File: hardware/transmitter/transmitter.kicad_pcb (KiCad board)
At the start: 2 copper layers, 69.1 x 53.8 mm, 25 parts, among them J1 Output

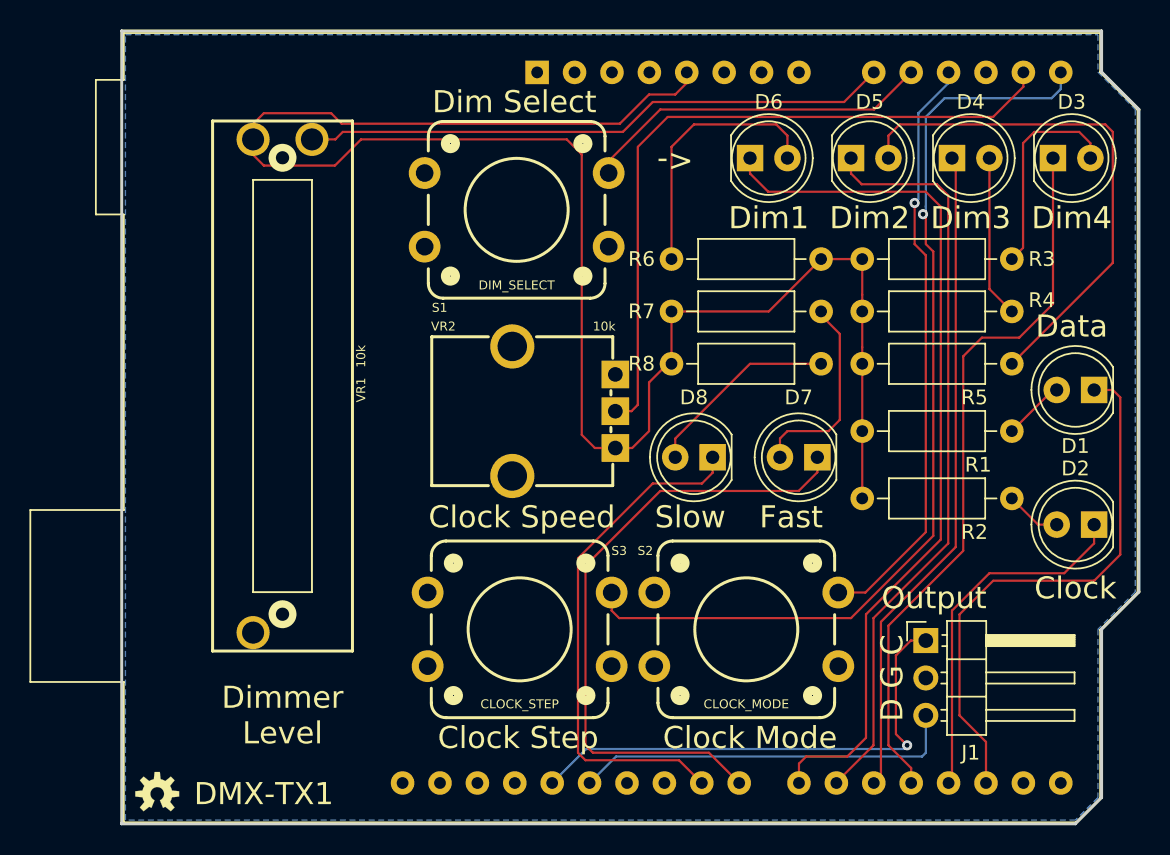
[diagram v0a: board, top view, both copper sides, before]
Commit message: Rev 1.1: - Fixed arduino shield footprint (it was backwards) - Added Fcu power plane - New Fcu layouts - Added rounded corners
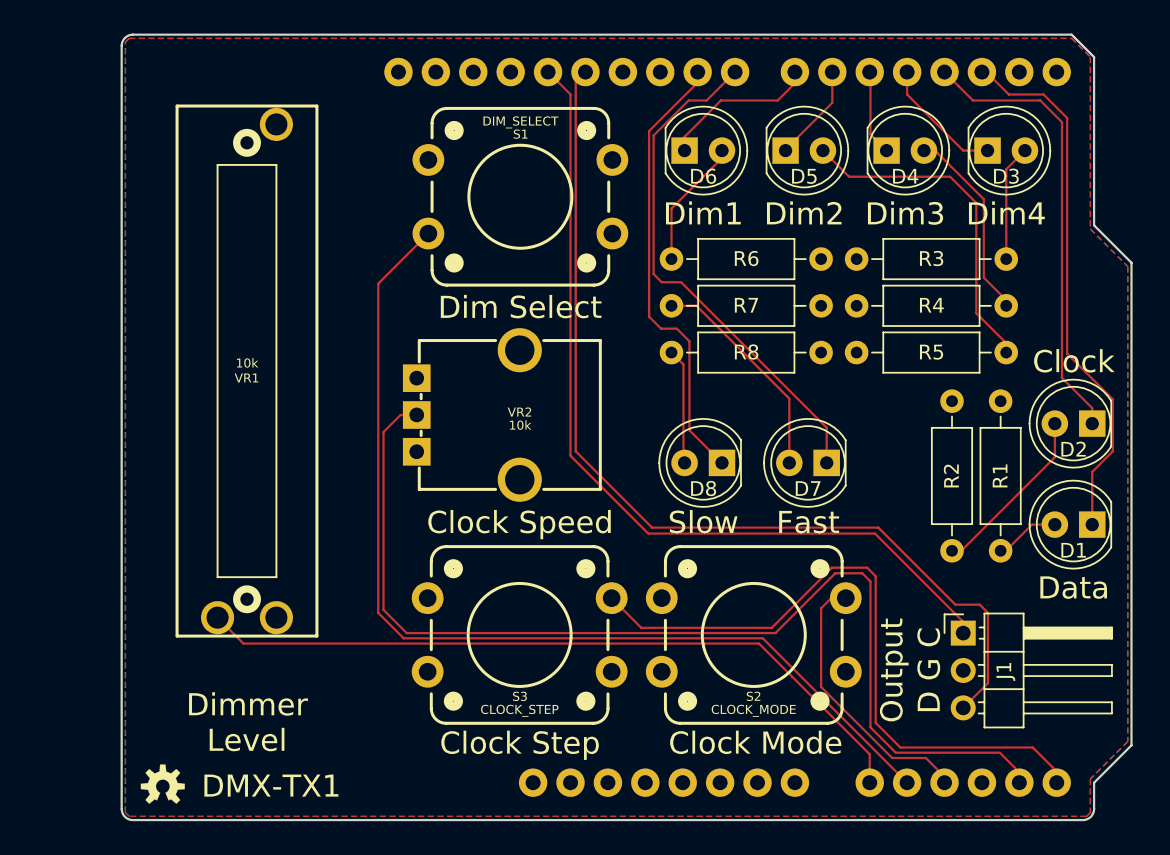
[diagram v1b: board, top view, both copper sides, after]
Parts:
- removed the ? at (118.7, 114.8)
- added ?: , footprints:OSHW-LOGO-S, F.Cu at (119.1, 114.3)
- A1: footprint Module:Arduino_UNO_R3 -> footprints:ARDUINO_R3_NO_HOLES
- moved A1 24.9 mm to (150.6, 89.9)
- moved R8 10.2 mm to (163.8, 84.8), turned to 180 degrees
- moved R7 10.2 mm to (163.8, 81.7), turned to 180 degrees
- moved R1 9.62 mm to (176.0, 88.1), turned to 270 degrees
- moved D1 9.14 mm to (182.2, 96.5)
- moved R2 8.99 mm to (172.7, 88.1), turned to 270 degrees
- moved D2 6.86 mm to (182.2, 89.7)
- moved D3 4.47 mm to (175.1, 71.1)
- moved D4 4.47 mm to (168.3, 71.1)
- moved D5 4.47 mm to (161.4, 71.1)
- moved D6 4.47 mm to (154.6, 71.1)
- moved VR1 2.62 mm to (124.8, 86.1), turned to 90 degrees
- moved J1 2.59 mm to (173.5, 103.9)
- moved S1 0.92 mm to (143.4, 74.3), turned to 180 degrees
- moved R5 0.85 mm to (166.2, 84.8)
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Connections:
- VR1 pad BOTT: GND -> +5V
- VR1 pad TOP: +5V -> GND
- VR2 pad P$1: +5V -> GND
- VR2 pad P$3: GND -> +5V
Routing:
- net +5V: track 121.9 -> 0.43 mm
- net /~DIM0: track 59.7 -> 10.7 mm
- net /A1: track 23.9 -> 68.7 mm
- net /~DIM1: track 51.3 -> 6.65 mm
- net /~DIM3: track 49.2 -> 8.56 mm
- net /RX: track 26.2 -> 65.7 mm
- net /~DIM2: track 44.9 -> 5.81 mm
- net /RXCLK: track 34.0 -> 59.4 mm, vias 1 -> 0
- net /A4: track 48.1 -> 72.4 mm
- net /A2: track 41.0 -> 18.6 mm, vias 1 -> 0
- net /A5: track 65.5 -> 46.0 mm, vias 1 -> 0
- net Net-(D5-Pad2): track 35.9 -> 22.9 mm
- net /A0: track 40.0 -> 50.1 mm
- net Net-(D6-Pad2): track 18.0 -> 8.79 mm
- net /~CLK_SLO: track 43.8 -> 35.2 mm
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- added copper zone on F.Cu, net +5V
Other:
- board size 69.1 x 53.8 mm -> 68.6 x 53.3 mm
- net class Power added: clearance 0.1524, trace_width 0.3048, via_dia 1.27, via_drill 0.635
- board text added: "DMX-TX1, Rev 1.1 Crazy Giraffe Software"
- board text removed: "->"
- board text removed: "DMX-TX1, Rev 1.0 Crazy Giraffe Software"

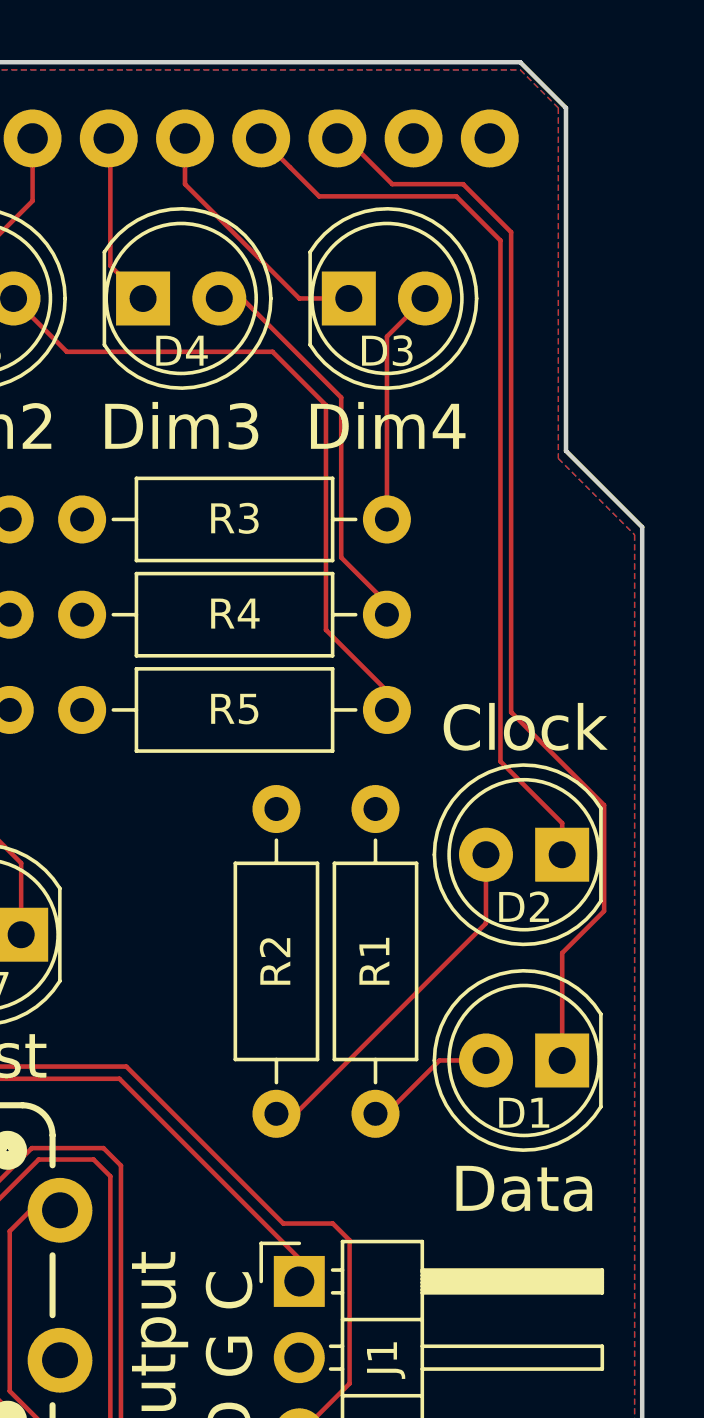
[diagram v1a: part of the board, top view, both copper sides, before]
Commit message: Users/sparky/txrx12 (#11)
* TX1 1.2, RX1 1.2
Move Clock LED to avoid ICSP connector.
Align TX Fast/Slo clock LEDS and RX start code/error LEDs.

* Add RXCLK to D9 connection for Leonardo PCINT5.

Co-authored-by: SparkyBobo <sparky@crazygiraffesoftware.com>
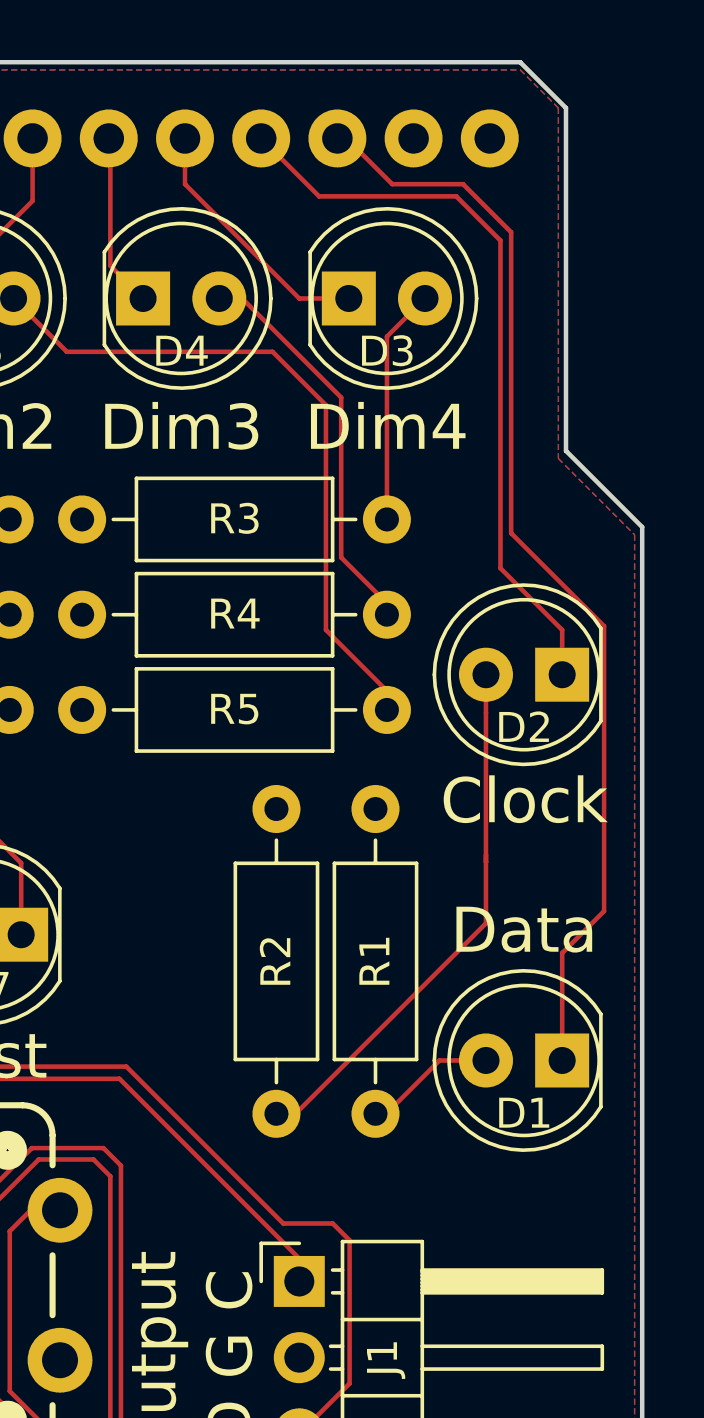
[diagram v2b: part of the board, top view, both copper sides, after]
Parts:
- D7: value CLK_SLO -> CLK_FST
- D8: value CLK_FST -> CLK_SLO
- moved D2 6.00 mm to (182.2, 83.7)
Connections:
- A1 pad 23: /~CLK_SLO -> /~CLK_FST
- A1 pad 24: /~CLK_FST -> /~CLK_SLO
- D7 pad 1: /~CLK_SLO -> /~CLK_FST
- D8 pad 1: /~CLK_FST -> /~CLK_SLO
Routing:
- net Net-(D2-Pad2): track 11.9 -> 18.2 mm
- net /~CLOCK: track 30.7 -> 24.7 mm
- net /~CLK_SLO: track 35.2 -> 30.6 mm
- net /~CLK_FST: track 30.6 -> 35.2 mm
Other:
- board text added: "DMX-TX1, Rev 1.2 Crazy Giraffe Software"
- board text removed: "DMX-TX1, Rev 1.1 Crazy Giraffe Software"
